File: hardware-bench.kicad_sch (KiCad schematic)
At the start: 3 parts

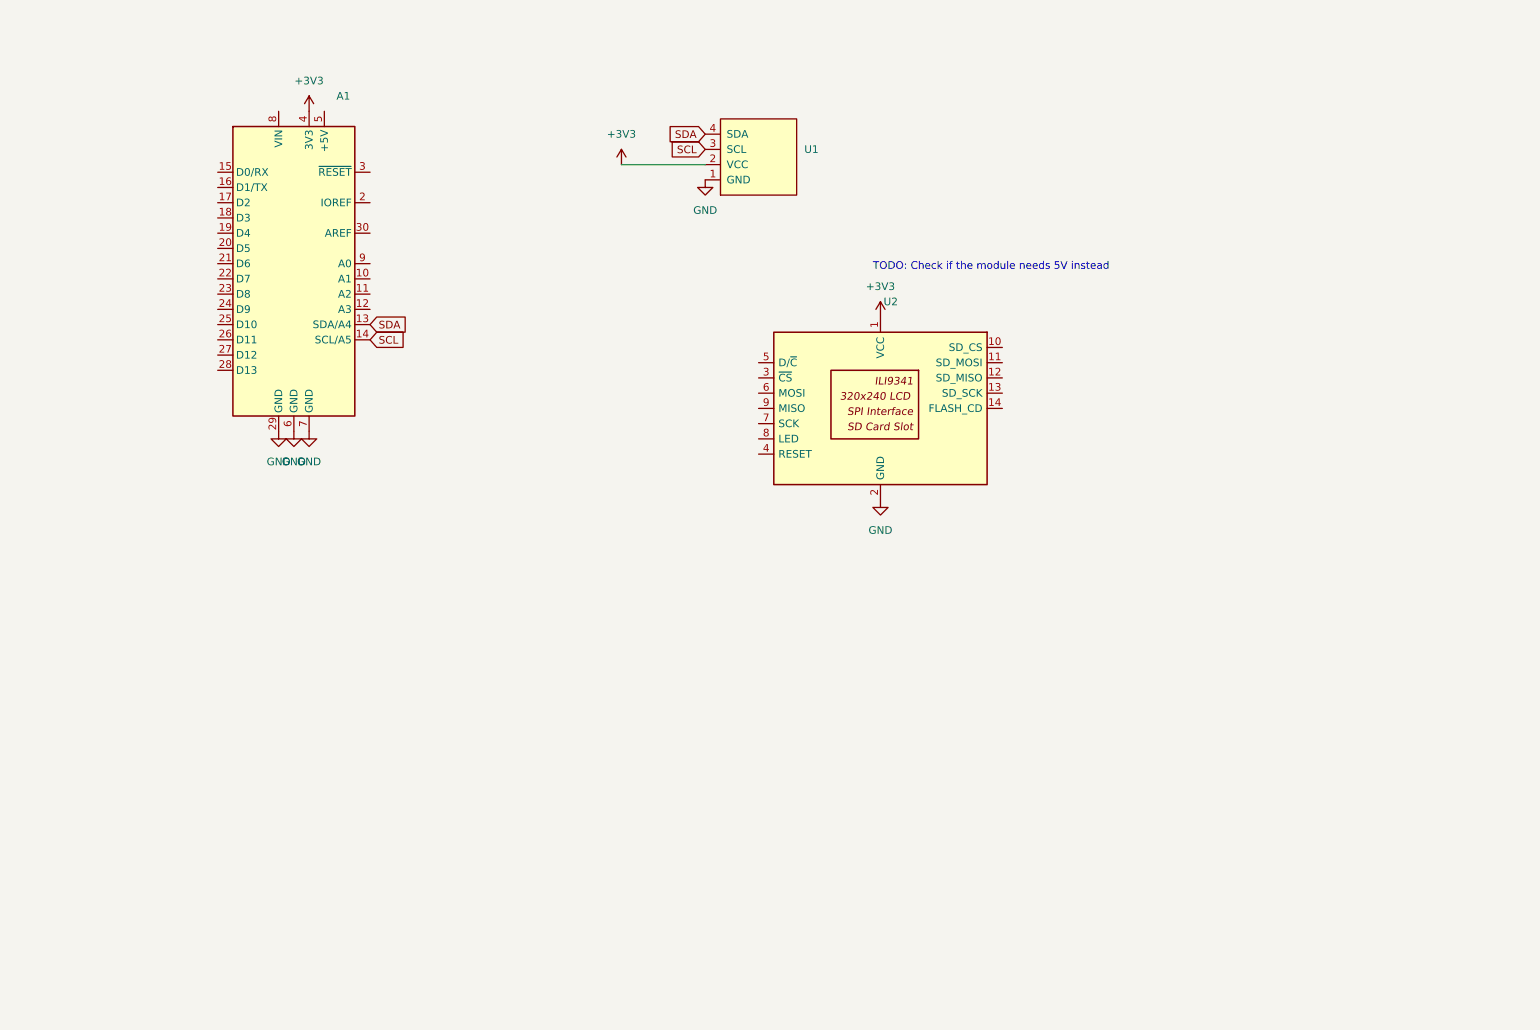
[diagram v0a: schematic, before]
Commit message: Raspberry PI Pico hardware bench (#2)
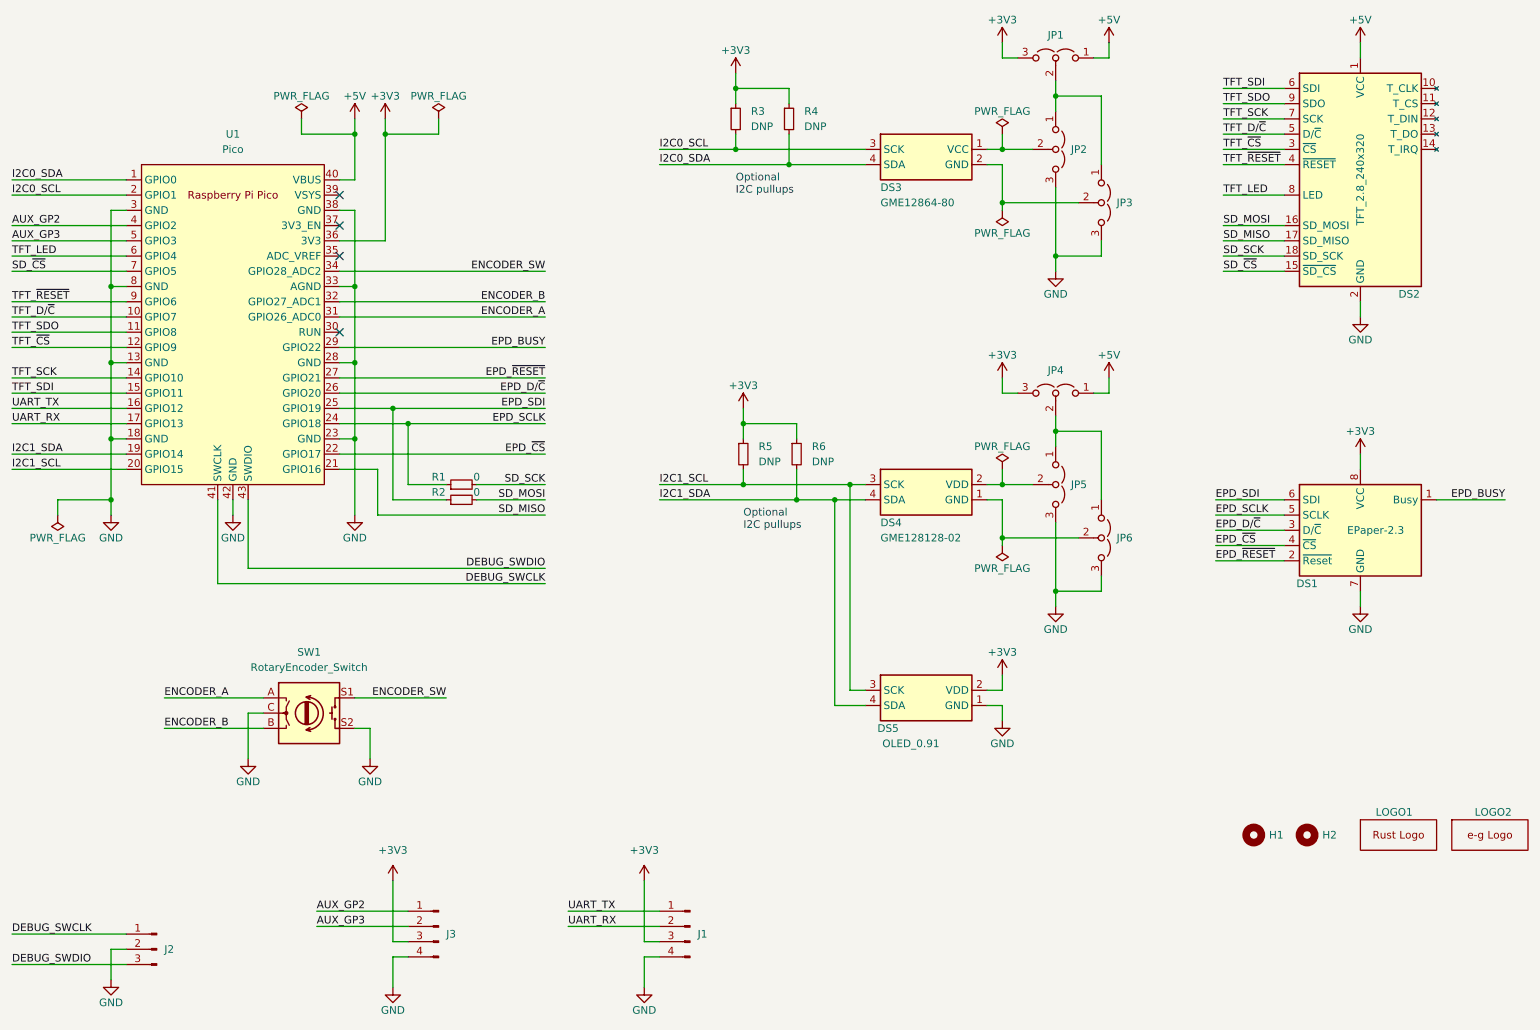
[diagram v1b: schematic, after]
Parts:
- removed A1: (no value), symbol MCU_Module:Arduino_UNO_R2
- removed U1: (no value), symbol SSD1306-128x64_OLED:SSD1306
- removed U2: (no value), symbol Driver_Display:CR2013-MI2120
- added DS1: EPaper-2.3, hardware-bench:EPaper-2.13, symbol hardware-bench:EPaper-2.3
- added DS2: TFT_2.8_240x320, hardware-bench:TFT_2.8_240x320, symbol hardware-bench:TFT_2.8_240x320
- added DS3: GME12864-80, hardware-bench:GME12864-80, symbol hardware-bench:GME12864-80
- added DS4: GME128128-02, hardware-bench:GME128128-02, symbol hardware-bench:GME128128-02
- added DS5: OLED_0.91, hardware-bench:OLED_0.91, symbol hardware-bench:OLED_0.91
- added H1, H2: MountingHole, MountingHole:MountingHole_3.2mm_M3, symbol Mechanical:MountingHole
- added J1, J3: Conn_01x04_Male, hardware-bench:PinHeader_1x04_P2.54mm_Horizontal_Flipped, symbol Connector:Conn_01x04_Male
- added J2: Conn_01x03_Male, hardware-bench:PinHeader_1x03_P2.54mm_Horizontal_Flipped, symbol Connector:Conn_01x03_Male
- added JP1, JP2, JP3, JP4, JP5, JP6: Jumper_3_Open, Connector_PinHeader_2.54mm:PinHeader_1x03_P2.54mm_Vertical, symbol Jumper:Jumper_3_Open
- added LOGO1: Logo_Rust, hardware-bench:Logo_Rust, symbol hardware-bench:Logo_Rust
- added LOGO2: Logo_E_G, hardware-bench:Logo_E_G, symbol hardware-bench:Logo_E_G
- added R1, R2: 0, Resistor_SMD:R_0603_1608Metric, symbol Device:R_Small
- added R3, R4, R5, R6: DNP, Resistor_SMD:R_0603_1608Metric, symbol Device:R_Small
- added SW1: RotaryEncoder_Switch, Rotary_Encoder:RotaryEncoder_Alps_EC12E-Switch_Vertical_H20mm_CircularMountingHoles, symbol Device:RotaryEncoder_Switch
- added U1: Pico, hardware-bench:RPi_Pico_SMD, symbol hardware-bench:Pico
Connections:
- net +3V3: now also DS1.8 (VCC), DS5.2 (VDD), J1.3 (Pin_3), J3.3 (Pin_3), JP1.3 (B), JP4.3 (B), R3.1, R4.1, R5.1, R6.1, U1.36 (3V3)
- net GND: now also DS1.7 (GND), DS2.2 (GND), DS5.1 (GND), J1.4 (Pin_4), J2.2 (Pin_2), J3.4 (Pin_4), JP2.3 (B), JP3.3 (B), JP5.3 (B), JP6.3 (B), SW1.C, SW1.S2, U1.13 (GND), U1.18 (GND), U1.23 (GND), U1.28 (GND), U1.3 (GND), U1.33 (AGND), U1.38 (GND), U1.42 (GND), U1.8 (GND)
- new net: JP1.2 (C), JP2.1 (A), JP3.1 (A)
- new net: DS3.2 (GND), JP3.2 (C)
- new net: JP4.2 (C), JP5.1 (A), JP6.1 (A)
- new net: DS3.1 (VCC), JP2.2 (C)
- new net: DS4.2 (VDD), JP5.2 (C)
- new net: DS4.1 (GND), JP6.2 (C)
- new net +5V: DS2.1 (VCC), JP1.1 (A), JP4.1 (A), U1.40 (VBUS)
- new net AUX_GP2: J3.1 (Pin_1), U1.4 (GPIO2)
- new net AUX_GP3: J3.2 (Pin_2), U1.5 (GPIO3)
- new net DEBUG_SWCLK: J2.1 (Pin_1), U1.41 (SWCLK)
- new net DEBUG_SWDIO: J2.3 (Pin_3), U1.43 (SWDIO)
- new net ENCODER_A: SW1.A, U1.31 (GPIO26_ADC0)
- new net ENCODER_B: SW1.B, U1.32 (GPIO27_ADC1)
- new net ENCODER_SW: SW1.S1, U1.34 (GPIO28_ADC2)
- new net EPD_BUSY: DS1.1 (Busy), U1.29 (GPIO22)
- new net EPD_D/~{C}: DS1.3 (D/~{C}), U1.26 (GPIO20)
- new net EPD_SCLK: DS1.5 (SCLK), R1.1, U1.24 (GPIO18)
- new net EPD_SDI: DS1.6 (SDI), R2.1, U1.25 (GPIO19)
- new net EPD_~{CS}: DS1.4 (~{CS}), U1.22 (GPIO17)
- new net EPD_~{RESET}: DS1.2 (~{Reset}), U1.27 (GPIO21)
- new net I2C0_SCL: DS3.3 (SCK), R3.2, U1.2 (GPIO1)
- new net I2C0_SDA: DS3.4 (SDA), R4.2, U1.1 (GPIO0)
- new net I2C1_SCL: DS4.3 (SCK), DS5.3 (SCK), R5.2, U1.20 (GPIO15)
- new net I2C1_SDA: DS4.4 (SDA), DS5.4 (SDA), R6.2, U1.19 (GPIO14)
- new net SD_MISO: DS2.17 (SD_MISO), U1.21 (GPIO16)
- new net SD_MOSI: DS2.16 (SD_MOSI), R2.2
- new net SD_SCK: DS2.18 (SD_SCK), R1.2
- new net SD_~{CS}: DS2.15 (~{SD_CS}), U1.7 (GPIO5)
- new net TFT_D/~{C}: DS2.5 (D/~{C}), U1.10 (GPIO7)
- new net TFT_LED: DS2.8 (LED), U1.6 (GPIO4)
- new net TFT_SCK: DS2.7 (SCK), U1.14 (GPIO10)
- new net TFT_SDI: DS2.6 (SDI), U1.15 (GPIO11)
- new net TFT_SDO: DS2.9 (SDO), U1.11 (GPIO8)
- new net TFT_~{CS}: DS2.3 (~{CS}), U1.12 (GPIO9)
- new net TFT_~{RESET}: DS2.4 (~{RESET}), U1.9 (GPIO6)
- new net UART_RX: J1.2 (Pin_2), U1.17 (GPIO13)
- new net UART_TX: J1.1 (Pin_1), U1.16 (GPIO12)
- no-connect marks 0 -> 4
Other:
- note added: "Optional I2C pullups"
- note removed: "TODO: Check if the module needs 5V instead"
- title: (none) -> Embedded-graphics hardware bench
